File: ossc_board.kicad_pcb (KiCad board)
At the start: 2 copper layers, 90 x 167 mm, 323 parts, among them J1 HDMI_CONN (10029449-111RLF), J10 COLOR INPUT, J11 MONO INPUT, J12 NEXT PWR INPUT 1, J13 NEXT PWR INPUT 2, J14 -12VDC OUT, J15 5VDC STANDBY, J16 MON IN 1, J17 MON IN 2, J18 PA1, J19 BOOT0, J2 OUT (SJ1-3535NG), J20 PC0, J21 PC1, J22 PB0, J23 PB1, J24 R SPK, J25 R SPEAKER (SJ-2509N), J26 L SPEAKER, J27 L SPK, J3 MIC (SJ1-3535NG), J31 NeXT Keyboard, J32 NeXT Keyboard (MD-50SM / KMDG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, J4 USB Host (SS-52100-001), J5 Mic IN, J6 Audio OUT, J7 STLINK, J8 UART2, J9 PA0, P1 JTAG (30310-6002HB), Q1 2SC2712, SW1 NeXT POWER SW (1-1825027-1 / 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, SW2 BTN0, SW3 NeXT POWER SW, SW4 RESET, U1 TVP7002PZP, U10 S25FL216K (IS25LP016D-JBLE), U11 TLV70033DDCR, U12 TLV70012DDCT, U13 TLV70025DDCT, U14 TLV70012DDCT, U15 TLV70018DDCT, U16 TLV70018DDCT, U17 USBLC6-2SC6, U18 STMPS2141STR, U19 SN74LVC2G34DBV, U2 EP4CE15E22C8N, U20 PCM5122PW, U21 TLV70033DDCR, U22 TLV70033DDCR, U23 PLT133/T, U24 STM32F401RCT6, U25 SN74LVC1G07DBV, U26 SN74HCT125DR, U27 TLV320ADC3100, U28 BD33FC0FP, U29 TPA2005D1DGN, U3 IT6613E, U30 BD33FC0FP, U31 TPA2005D1DGN, U4 SN74LVC2G17DBV, U5 BD33FC0FP, U6 TLV70033DDCR, U7 NCP703SN19T1G, U8 5V(DC/DC), U9 TLV70019DDCT, X1 ACHL-27MHZ-EK, X2 ASEDV-27.000MHZ-LR-T(ECS-2333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, X3 ECS-2520MVLC-225.792-BN-TR, Y2 25MHz (FA-238 25.0000MB-K0)

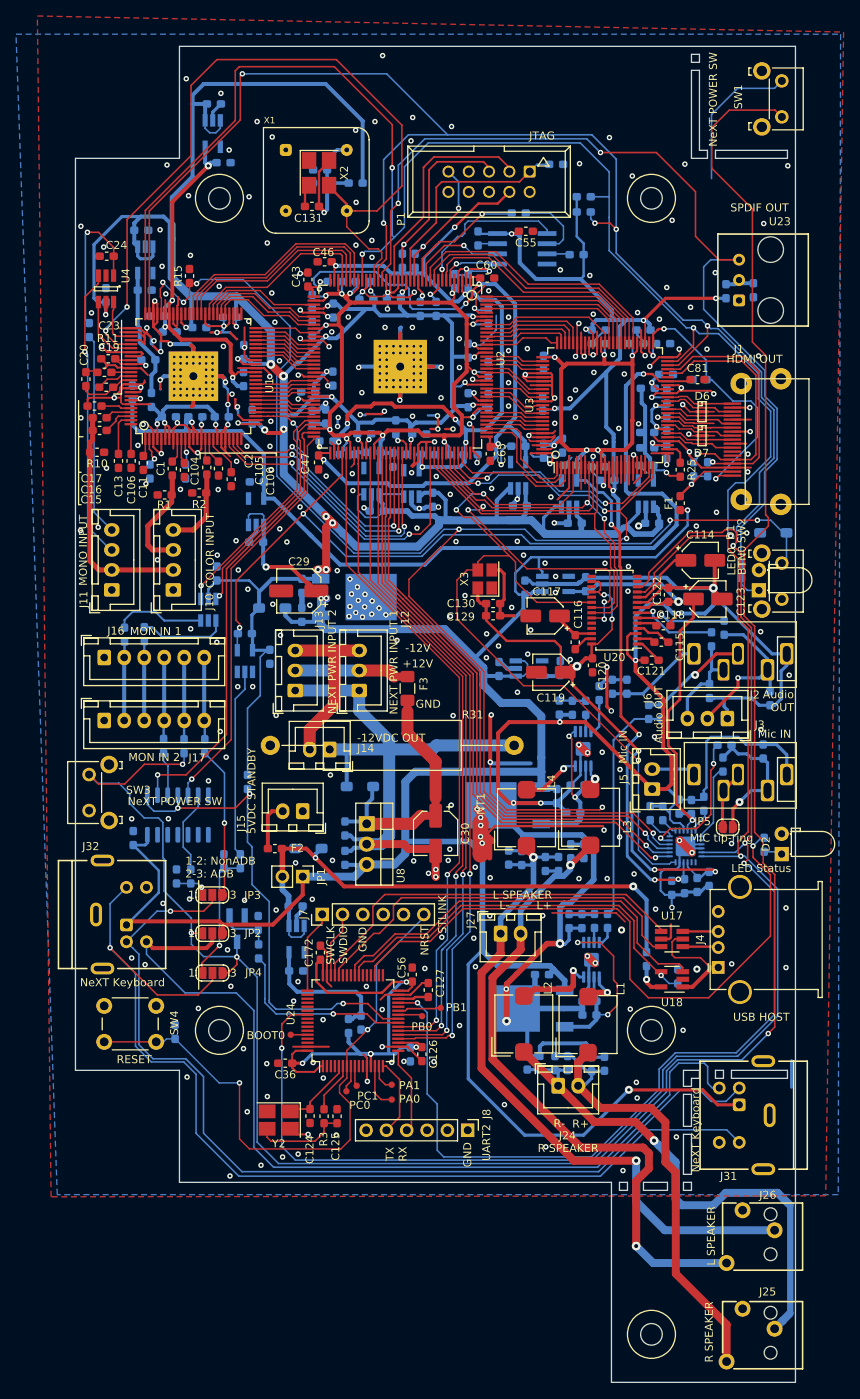
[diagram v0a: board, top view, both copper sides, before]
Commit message: add optional components
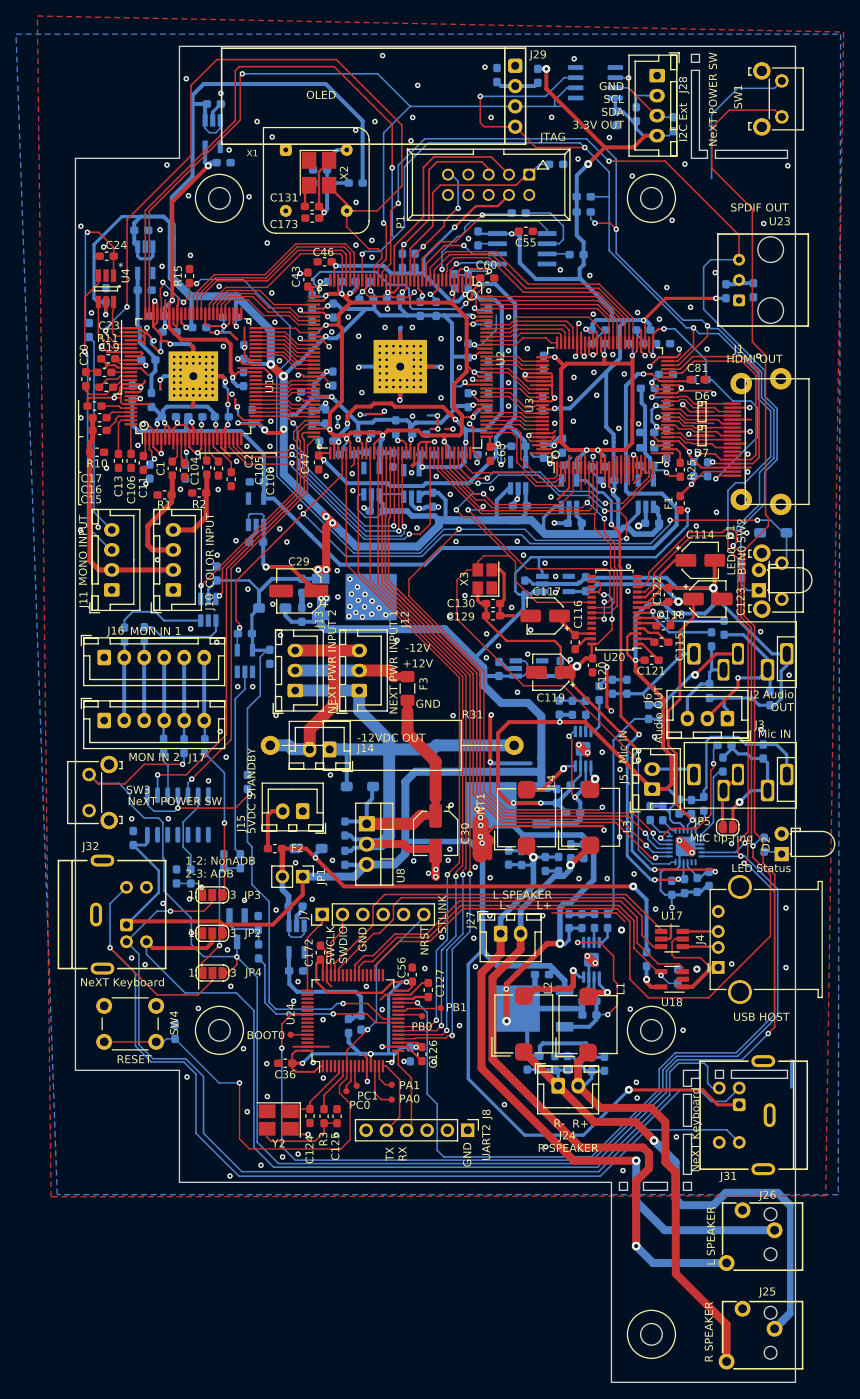
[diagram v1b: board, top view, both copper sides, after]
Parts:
- added C173: 1u, Capacitor_SMD:C_0603_1608Metric_Pad1.05x0.95mm_HandSolder, F.Cu at (68.3, 53.5)
- added C174: 0.1u, Capacitor_SMD:C_0603_1608Metric_Pad1.05x0.95mm_HandSolder, B.Cu at (106.3, 41.0)
- added C175: 0.1u, Capacitor_SMD:C_0603_1608Metric_Pad1.05x0.95mm_HandSolder, B.Cu at (91.4, 35.6)
- added FB10: MPZ1608S221A, Inductor_SMD:L_0603_1608Metric_Pad1.05x0.95mm_HandSolder, B.Cu at (96.5, 35.7)
- added J28: I2C Ext, Connector_JST:JST_XH_B4B-XH-A_1x04_P2.50mm_Vertical, F.Cu at (111.4, 35.7)
- added J29: OLED, custom_components:OLED_0.91inch_I2C, F.Cu at (93.7, 34.4)
- added R47: (10k), Resistor_SMD:R_0603_1608Metric_Pad1.05x0.95mm_HandSolder, B.Cu at (108.8, 40.5)
- added R48: (10k), Resistor_SMD:R_0603_1608Metric_Pad1.05x0.95mm_HandSolder, B.Cu at (113.4, 41.7)
- added U32: PCA9515D, Package_SO:SOIC-8_3.9x4.9mm_P1.27mm, B.Cu at (103.7, 36.6)
- C128: value 0.01u -> 0.1u
- R36: value 10k -> 47k
- moved P1 0.38 mm to (90.3, 49.3)
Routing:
- net VCC: track 546.6 -> 586.2 mm, vias 31 -> 33
- net /fpga1/SDA: track 360.2 -> 390.7 mm, vias 6 -> 8
- net Net-(J28-Pad3): track 0.00 -> 10.1 mm, vias 0 -> 1
- net Net-(J28-Pad2): track 0.00 -> 7.09 mm
- net Net-(C175-Pad1): track 0.00 -> 5.48 mm
- net /soundbox/-12V: track 22.4 -> 27.5 mm
- net /fpga1/SCL: track 342.8 -> 345.7 mm
- net /soundbox/SPDIF: track 116.2 -> 114.8 mm
- net Net-(C131-Pad2): track 19.7 -> 20.7 mm
- net GND: vias 338 -> 344
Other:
- board text added: "*"
- board text added: "GND SCL SDA 3.3V OUT"

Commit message: update
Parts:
- moved C91 0.27 mm to (83.4, 89.0)
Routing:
- net GND: track 738.4 -> 747.4 mm, vias 344 -> 349
- net /fpga1/SCL: track 345.7 -> 344.3 mm
- net Net-(J31-Pad4): track 113.8 -> 112.8 mm
- net /fpga1/SDA: track 390.7 -> 389.8 mm
- net /fpga1/HDMITX_INT_N: track 30.5 -> 31.5 mm
- net /soundbox/N_RESET: track 197.1 -> 197.9 mm
- net /fpga1/AudioOut_MCLK: track 110.2 -> 110.9 mm
- net /soundbox/NRST: track 75.1 -> 74.4 mm
- net /fpga1/VCCD_PLL: track 93.2 -> 92.6 mm

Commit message: minor update
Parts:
- R31: value 120 5W -> 2x 120 5W (or 56ohm 7W)
- R34: value 10k -> 4.7k
- SW4: value RESET -> MCU RESET
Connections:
- U17 pad 2: GND -> Net-(U17-Pad2)
- U17 pad 4: Net-(J4-Pad2) -> Net-(U17-Pad4)
- U17 pad 5: Net-(J4-Pad1) -> Net-(U17-Pad5)
- U17 pad 6: Net-(J4-Pad3) -> Net-(U17-Pad6)
- U24 pad 44: Net-(U17-Pad3) -> Net-(U24-Pad44)
- U24 pad 45: Net-(U17-Pad1) -> Net-(U24-Pad45)
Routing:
- net Net-(U17-Pad2): track 0.00 -> 2.92 mm
- net GND: track 747.4 -> 744.5 mm

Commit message: update values
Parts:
- added R49: 22-150, Resistor_SMD:R_0603_1608Metric_Pad1.05x0.95mm_HandSolder, B.Cu at (46.4, 97.4)
- C11: value 0.01u -> 0.01u (GCM188R72A103KA37J)
- C112: value 2200p -> 2200p (GRM1885C1H222JA01J)
- C115: value 2.2u -> 2.2u (GRM188R71A225KE15D)
- C3: value 1u -> 1u (GRT188R61H105KE13D)
- C31: value 10u -> 10u (ZRB18AR61E106ME01L)
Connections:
- J11 pad 2: /soundbox/GREEN_OUT -> /soundbox/MONO_VIDEO
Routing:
- net /soundbox/MONO_VIDEO: track 0.00 -> 2.24 mm
- net GND: vias 349 -> 351
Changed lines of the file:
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@@
     (thickness 1.6)
     (drawings 136)
-    (tracks 4577)
+    (tracks 4584)
     (zones 0)
-    (modules 332)
-    (nets 319)
+    (modules 333)
+    (nets 320)
   )
   (page A4)
@@
     (35 F.Paste user hide)
     (36 B.SilkS user)
-    (37 F.SilkS user)
+    (37 F.SilkS user hide)
     (38 B.Mask user hide)
-    (39 F.Mask user)
+    (39 F.Mask user hide)
     (40 Dwgs.User user)
     (41 Cmts.User user)
@@
     (47 F.CrtYd user hide)
     (48 B.Fab user hide)
-    (49 F.Fab user)
+    (49 F.Fab user hide)
   )
   (setup
@@
   (net 317 "Net-(U24-Pad45)")
   (net 318 "Net-(U24-Pad44)")
+  (net 319 /soundbox/MONO_VIDEO)
   (net_class Default "This is the default net class."
     (clearance 0.2)
@@
     (add_net /soundbox/MIC_DATA)
     (add_net /soundbox/MIC_LRCK)
+    (add_net /soundbox/MONO_VIDEO)
     (add_net /soundbox/MON_CLK_)
     (add_net /soundbox/MON_IN)
@@
     (add_net /tvp_board1/VSYNC)
   )
+  (module Resistor_SMD:R_0603_1608Metric_Pad1.05x0.95mm_HandSolder (layer B.Cu)
+    (at 46.355 97.4344)
+    (descr "Resistor SMD 0603 (1608 Metric), square (rectangular) end terminal, IPC_7351 nominal with elongated pad for handsoldering. (Body size source: http://www.tortai-tech.com/upload/download/2011102023233369053.pdf), generated with kicad-footprint-generator")
+    (tags "resistor handsolder")
+    (attr smd)
+    (fp_text reference R49 (at 0 1.43) (layer B.SilkS)
+      (effects (font (size 1 1) (thickness 0.15)) (justify mirror))
+    )
+    (fp_text value 22-150 (at 0 -1.43) (layer B.Fab)
+      (effects (font (size 1 1) (thickness 0.15)) (justify mirror))
+    )
+    (fp_line (start 1.65 -0.73) (end -1.65 -0.73) (layer B.CrtYd) (width 0.05))
+    (fp_line (start 1.65 0.73) (end 1.65 -0.73) (layer B.CrtYd) (width 0.05))
+    (fp_line (start -1.65 0.73) (end 1.65 0.73) (layer B.CrtYd) (width 0.05))
+    (fp_line (start -1.65 -0.73) (end -1.65 0.73) (layer B.CrtYd) (width 0.05))
+    (fp_line (start -0.171267 -0.51) (end 0.171267 -0.51) (layer B.SilkS) (width 0.12))
+    (fp_line (start -0.171267 0.51) (end 0.171267 0.51) (layer B.SilkS) (width 0.12))
+    (fp_line (start 0.8 -0.4) (end -0.8 -0.4) (layer B.Fab) (width 0.1))
+    (fp_line (start 0.8 0.4) (end 0.8 -0.4) (layer B.Fab) (width 0.1))
+    (fp_line (start -0.8 0.4) (end 0.8 0.4) (layer B.Fab) (width 0.1))
+    (fp_line (start -0.8 -0.4) (end -0.8 0.4) (layer B.Fab) (width 0.1))
+    (fp_text user %R (at 0 0) (layer B.Fab)
+      (effects (font (size 0.4 0.4) (thickness 0.06)) (justify mirror))
+    )
+    (pad 2 smd roundrect (at 0.875 0) (size 1.05 0.95) (layers B.Cu B.Paste B.Mask) (roundrect_rratio 0.25)
+      (net 143 /soundbox/GREEN_OUT))
+    (pad 1 smd roundrect (at -0.875 0) (size 1.05 0.95) (layers B.Cu B.Paste B.Mask) (roundrect_rratio 0.25)
+      (net 319 /soundbox/MONO_VIDEO))
+    (model ${KISYS3DMOD}/Resistor_SMD.3dshapes/R_0603_1608Metric.wrl
+      (at (xyz 0 0 0))
+      (scale (xyz 1 1 1))
+      (rotate (xyz 0 0 0))
+    )
+  )
   (module custom_components:OLED_0.91inch_I2C (layer F.Cu)
     (at 93.6708 34.4234 180)
@@
       (effects (font (size 1 1) (thickness 0.15)))
     )
-    (fp_text value 2.2u (at 0 1.43) (layer F.Fab)
+    (fp_text value "2.2u (GRM188R71A225KE15D)" (at 0 1.43) (layer F.Fab)
       (effects (font (size 1 1) (thickness 0.15)))
     )
@@
       (effects (font (size 1 1) (thickness 0.15)) (justify mirror))
     )
-    (fp_text value 2200p (at 0 -1.43 90) (layer B.Fab)
+    (fp_text value "2200p (GRM1885C1H222JA01J)" (at 0 -1.43 90) (layer B.Fab)
       (effects (font (size 1 1) (thickness 0.15)) (justify mirror))
     )
@@
       (net 146 /soundbox/HS_OUT))
     (pad 2 thru_hole oval (at 2.5 0 90) (size 1.7 1.95) (drill 0.95) (layers *.Cu *.Mask)
-      (net 143 /soundbox/GREEN_OUT))
+      (net 319 /soundbox/MONO_VIDEO))
     (pad 1 thru_hole roundrect (at 0 0 90) (size 1.7 1.95) (drill 0.95) (layers *.Cu *.Mask) (roundrect_rratio 0.147059)
       (net 87 GND))
@@
       (effects (font (size 1 1) (thickness 0.15)) (justify mirror))
     )
-    (fp_text value 1u (at 0 -1.43) (layer B.Fab)
+    (fp_text value "1u (GRT188R61H105KE13D)" (at 0 -1.43) (layer B.Fab)
       (effects (font (size 1 1) (thickness 0.15)) (justify mirror))
     )
@@
       (effects (font (size 1 1) (thickness 0.15)) (justify mirror))
     )
-    (fp_text value 10u (at 0 -1.43 270) (layer B.Fab)
+    (fp_text value "10u (ZRB18AR61E106ME01L)" (at 0 -1.43 270) (layer B.Fab)
       (effects (font (size 1 1) (thickness 0.15)) (justify mirror))
     )
@@
       (effects (font (size 1 1) (thickness 0.15)))
     )
-    (fp_text value 0.01u (at 0 1.43 90) (layer F.Fab)
+    (fp_text value "0.01u (GCM188R72A103KA37J)" (at 0 1.43 90) (layer F.Fab)
       (effects (font (size 1 1) (thickness 0.15)))
     )
@@
   (via (at 57.7088 144.9324) (size 0.686) (drill 0.33) (layers F.Cu B.Cu) (net 87))
   (via (at 58.12028 149.49424) (size 0.686) (drill 0.33) (layers F.Cu B.Cu) (net 87))
-  (via (at 39.32936 92.51696) (size 0.686) (drill 0.33) (layers F.Cu B.Cu) (net 87))
+  (via (at 39.5986 92.964) (size 0.686) (drill 0.33) (layers F.Cu B.Cu) (net 87))
   (via (at 39.38016 78.44028) (size 0.686) (drill 0.33) (layers F.Cu B.Cu) (net 87))
   (via (at 40.70604 65.31864) (size 0.686) (drill 0.33) (layers F.Cu B.Cu) (net 87))
@@
   (via (at 51.82616 87.376) (size 0.686) (drill 0.33) (layers F.Cu B.Cu) (net 87))
   (via (at 48.95088 96.18472) (size 0.686) (drill 0.33) (layers F.Cu B.Cu) (net 87))
-  (via (at 41.53916 92.11564) (size 0.686) (drill 0.33) (layers F.Cu B.Cu) (net 87))
+  (via (at 41.2496 91.7448) (size 0.686) (drill 0.33) (layers F.Cu B.Cu) (net 87))
   (via (at 56.5404 87.40648) (size 0.686) (drill 0.33) (layers F.Cu B.Cu) (net 87))
   (via (at 58.84672 83.8708) (size 0.686) (drill 0.33) (layers F.Cu B.Cu) (net 87))
@@
   (via (at 112.395 160.9598) (size 0.686) (drill 0.33) (layers F.Cu B.Cu) (net 87))
   (via (at 124.0028 133.7056) (size 0.686) (drill 0.33) (layers F.Cu B.Cu) (net 87))
+  (via (at 44.5262 90.6526) (size 0.686) (drill 0.33) (layers F.Cu B.Cu) (net 87))
+  (via (at 48.9712 93.4212) (size 0.686) (drill 0.33) (layers F.Cu B.Cu) (net 87))
   (segment (start 51.435 83.2625) (end 50.8 83.8975) (width 0.2) (layer F.Cu) (net 88))
   (segment (start 51.435 81.0308) (end 51.435 83.2625) (width 0.2) (layer F.Cu) (net 88))
@@
   (segment (start 40.8445 81.2025) (end 40.8445 80.01) (width 0.64) (layer F.Cu) (net 143))
   (segment (start 40.527 81.52) (end 40.8445 81.2025) (width 0.64) (layer F.Cu) (net 143))
-  (segment (start 40.513 96.3335) (end 41.6285 97.449) (width 0.64) (layer F.Cu) (net 143))
-  (segment (start 40.513 83.3295) (end 40.513 96.3335) (width 0.64) (layer F.Cu) (net 143))
+  (segment (start 40.513 83.3295) (end 40.513 84.963) (width 0.64) (layer F.Cu) (net 143))
+  (segment (start 40.513 84.963) (end 45.6946 90.1446) (width 0.64) (layer F.Cu) (net 143))
   (segment (start 40.527 83.3155) (end 40.513 83.3295) (width 0.64) (layer F.Cu) (net 143))
-  (segment (start 41.6285 97.449) (end 43.2435 97.449) (width 0.64) (layer F.Cu) (net 143))
   (segment (start 40.527 82.7405) (end 40.527 83.3155) (width 0.64) (layer F.Cu) (net 143))
-  (segment (start 43.2435 97.449) (end 50.927 97.449) (width 0.64) (layer F.Cu) (net 143))
+  (segment (start 47.8682 97.449) (end 50.927 97.449) (width 0.64) (layer F.Cu) (net 143))
+  (segment (start 45.6946 95.2754) (end 47.8682 97.449) (width 0.64) (layer F.Cu) (net 143))
+  (segment (start 45.6946 90.1446) (end 45.6946 95.2754) (width 0.64) (layer F.Cu) (net 143))
+  (segment (start 50.9124 97.4344) (end 50.927 97.449) (width 0.7) (layer B.Cu) (net 143))
+  (segment (start 47.23 97.4344) (end 50.9124 97.4344) (width 0.7) (layer B.Cu) (net 143))
   (segment (start 39.878 63.3238) (end 39.878 69.682425) (width 0.2) (layer F.Cu) (net 146))
   (segment (start 39.878 69.682425) (end 39.878 70.1675) (width 0.2) (layer F.Cu) (net 146))
@@
   (segment (start 111.9086 143.5862) (end 112.92148 143.5862) (width 0.3) (layer F.Cu) (net 316))
   (segment (start 113.1316 143.37608) (end 113.1316 141.76248) (width 0.3) (layer F.Cu) (net 316))
+  (segment (start 43.2581 97.4344) (end 43.2435 97.449) (width 0.7) (layer B.Cu) (net 319))
+  (segment (start 45.48 97.4344) (end 43.2581 97.4344) (width 0.7) (layer B.Cu) (net 319))
   (zone (net 0) (net_name "") (layer F.Cu) (hatch edge 0.508)
     (connect_pads (clearance 0.16))

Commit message: update
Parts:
- added R50: 10k, Resistor_SMD:R_0603_1608Metric_Pad1.05x0.95mm_HandSolder, F.Cu at (62.9, 150.4)
- C142, C143: value (0.1u) -> 0.1u
- R47, R48: value (10k) -> 10k
- U21, U22: value TLV70033DDCR -> TLV70033DDCR (or XC6204B332MR-G)
- moved R13 109.2 mm to (70.8, 155.4), turned to 270 degrees
- moved R14 101.9 mm to (75.3, 151.0)
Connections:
- R13 pad 1: /fpga1/SDA -> /soundbox/S_DVDD
- R13 pad 2: VCC -> /fpga1/SDA
- R14 pad 1: VCC -> /soundbox/S_DVDD
- U17 pad 2: Net-(U17-Pad2) -> GND
- U17 pad 4: Net-(U17-Pad4) -> Net-(J4-Pad2)
- U17 pad 5: Net-(U17-Pad5) -> Net-(J4-Pad1)
- U17 pad 6: Net-(U17-Pad6) -> Net-(J4-Pad3)
- U24 pad 44: Net-(U24-Pad44) -> Net-(U17-Pad3)
- U24 pad 45: Net-(U24-Pad45) -> Net-(U17-Pad1)
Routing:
- net VCC: track 586.2 -> 615.1 mm, vias 33 -> 34
- net Net-(R50-Pad2): track 0.00 -> 5.10 mm
- net /fpga1/SDA: track 389.8 -> 394.1 mm
- net GND: track 744.5 -> 747.4 mm, vias 351 -> 353
- net Net-(U17-Pad2): track 2.92 -> 0.00 mm
- net /soundbox/S_DVDD: track 17.8 -> 20.1 mm
- net Net-(C107-Pad1): track 65.4 -> 63.5 mm
- net /fpga1/SCL: track 344.3 -> 342.7 mm, vias 9 -> 8

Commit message: minor update
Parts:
- added D9: (RB160M-30TR), custom_components:D_SOD-123_HandSoldering, B.Cu at (81.8, 126.1)
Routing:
- net Net-(C30-Pad1): track 32.7 -> 35.0 mm, vias 0 -> 1
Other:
- board text added: "GND SCL SDA 3.3VOUT"
- board text removed: "GND SCL SDA 3.3V OUT"
